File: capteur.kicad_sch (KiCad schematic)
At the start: 14 parts, among them U1 MAX86141ENP+T, U2 ICM-20948

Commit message: Routage complet
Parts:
- removed C3: 100n, symbol Device:C
- removed D4, D5: VEMD5080X01, symbol Device:D_Photo
- removed U2: ICM-20948, Sensor_Motion:InvenSense_QFN-24_3x3mm_P0.4mm, symbol Sensor_Motion:ICM-20948
- added C31: 10n, Capacitor_SMD:C_0805_2012Metric, symbol Device:C
- added C33: 10µ, Capacitor_SMD:C_0805_2012Metric, symbol Device:C
- added D4, D6: VEMD8080, Local:XDCR_VEMD8080, symbol VEMD8080:VEMD8080
- added JP1: SolderJumper_2_Bridged, Jumper:SolderJumper-2_P1.3mm_Bridged2Bar_RoundedPad1.0x1.5mm, symbol Jumper:SolderJumper_2_Bridged
- added MT1: ICM-42670-P, Local:XDCR_ICM-42670-P, symbol ICM-42670-P:ICM-42670-P
- C1, C4, C5, C6, C7: footprint (none) -> Capacitor_SMD:C_0805_2012Metric
- C2: value 100n -> 2.2µ; footprint (none) -> Capacitor_SMD:C_0805_2012Metric
- D1, D2, D3: footprint (none) -> Local:CTDBLP31126C5D56J6U620R18
- U1: footprint 21-100134_N201A2-1_MXM -> Local:21-100134_N201A2-1_MXM
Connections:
- net +3.3V: now also C31.1, C33.1, MT1.12 (AP_CS), MT1.5 (VDDIO), MT1.8 (VDD)
- net GND: now also C31.2, JP1.2 (B), MT1.6 (GND); no longer U1.C5 (PD_GND)
- net ICM_AD0: now also MT1.1 (AP_SDO/AP_AD0)
- net ICM_FSYNC: now also MT1.7 (FSYNC)
- net ICM_INT: now also MT1.4 (INT1/INT)
- net SCL: now also MT1.13 (AP_SCL/AP_SCLK)
- net SDA: now also MT1.14 (AP_SDA/AP_SDIO/AP_SDI)
- net at U1.D5 (PD1_IN): now also D6.1, D6.2, D6.3, D6.4, D6.6, D6.7, D6.8
- net at U1.D4 (PD2_IN): now also D4.1, D4.2, D4.3, D4.4, D4.6, D4.7, D4.8
- net MAX_INT_1_8: no longer names the net of U1.B2 (*INT)
- new net ICM_INT2: MT1.9 (INT2)
- new net PD_GND: C33.2, D4.5, D6.5, JP1.1 (A), U1.C5 (PD_GND)
- no-connect marks 4 -> 8
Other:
- moved on the sheet: C1, C2, C5

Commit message: Set MPN
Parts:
- C1: JLCPCB Part # (none) -> CL21B104KBCNNNC; manf# CC1206KKX7R7BB105 -> CL21B104KBCNNNC
- C2: JLCPCB Part # (none) -> CL21B225KAFNNNE; manf# CC1206KKX7R7BB105 -> CL21B225KAFNNNE
- C31: JLCPCB Part # (none) -> CC0805JRNPO9BN100; manf# CC1206KKX7R7BB105 -> CC0805JRNPO9BN100
- C33, C4: JLCPCB Part # (none) -> CL21B106KPQNNNE; manf# CC1206KKX7R7BB105 -> CL21B106KPQNNNE
- C5: JLCPCB Part # (none) -> CL21B105KAFNFNE; manf# CC1206KKX7R7BB105 -> CL21B105KAFNFNE
- C6, C7: JLCPCB Part # (none) -> GRM21BZ71A226ME15L; manf# CC1206KKX7R7BB105 -> GRM21BZ71A226ME15L
- D1, D2, D3: value CT DBLP31.12-5C8C-56-J6Q6 -> CT DBLP31.12-6C5D-56-J6U6-20-R18; JLCPCB Part # (none) -> CT DBLP31.12-6C5D-56-J6U6-20-R18; manf# (none) -> CT DBLP31.12-6C5D-56-J6U6-20-R18
- D4, D6: JLCPCB Part # (none) -> VEMD8080; manf# (none) -> VEMD8080
- MT1: JLCPCB Part # (none) -> ICM-42670-P; manf# (none) -> ICM-42670-P
- U1: JLCPCB Part # (none) -> MAX86141ENP+T; manf# (none) -> MAX86141ENP+T
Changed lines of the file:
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@@
+			)
+		)
+		(property "manf#" "VEMD8080"
+			(at 167.64 152.4 90)
+			(effects
+				(font
+					(size 1.27 1.27)
+				)
+				(hide yes)
+			)
+		)
+		(property "JLCPCB Part #" "VEMD8080"
+			(at 167.64 152.4 90)
+			(effects
+				(font
+					(size 1.27 1.27)
+				)
+				(hide yes)
 			)
 		)
@@
 			)
 		)
+		(property "JLCPCB Part #" ""
+			(at 49.53 182.88 0)
+			(effects
+				(font
+					(size 1.27 1.27)
+				)
+				(hide yes)
+			)
+		)
 		(pin "1"
 		)
@@
 			)
 		)
-		(property "manf#" " CC1206KKX7R7BB105"
+		(property "manf#" "CL21B105KAFNFNE"
 			(at 130.81 104.14 0)
 			(effects
@@
 		)
 		(property "gp" " CC1206KKX7R7BB105"
+			(at 130.81 104.14 0)
+			(effects
+				(font
+					(size 1.27 1.27)
+				)
+				(hide yes)
+			)
+		)
+		(property "JLCPCB Part #" "CL21B105KAFNFNE"
 			(at 130.81 104.14 0)
 			(effects
@@
 			)
 		)
-		(property "manf#" " CC1206KKX7R7BB105"
+		(property "manf#" "CL21B106KPQNNNE"
 			(at 55.88 128.27 0)
 			(effects
@@
 		)
 		(property "gp" " CC1206KKX7R7BB105"
+			(at 55.88 128.27 0)
+			(effects
+				(font
+					(size 1.27 1.27)
+				)
+				(hide yes)
+			)
+		)
+		(property "JLCPCB Part #" "CL21B106KPQNNNE"
 			(at 55.88 128.27 0)
 			(effects
@@
 			)
 		)
-		(property "manf#" " CC1206KKX7R7BB105"
+		(property "manf#" "CL21B104KBCNNNC"
 			(at 129.54 29.21 0)
 			(effects
@@
 			)
 		)
+		(property "JLCPCB Part #" "CL21B104KBCNNNC"
+			(at 129.54 29.21 0)
+			(effects
+				(font
+					(size 1.27 1.27)
+				)
+				(hide yes)
+			)
+		)
 		(pin "2"
 		)
@@
 			)
 		)
-		(property "Value" "CT DBLP31.12-5C8C-56-J6Q6"
+		(property "Value" "CT DBLP31.12-6C5D-56-J6U6-20-R18"
 			(at 196.342 130.556 0)
 			(effects
@@
 		)
 		(property "Sim.Pins" "1=K 2=A"
+			(at 199.39 130.81 0)
+			(effects
+				(font
+					(size 1.27 1.27)
+				)
+				(hide yes)
+			)
+		)
+		(property "manf#" "CT DBLP31.12-6C5D-56-J6U6-20-R18"
+			(at 199.39 130.81 0)
+			(effects
+				(font
+					(size 1.27 1.27)
+				)
+				(hide yes)
+			)
+		)
+		(property "JLCPCB Part #" "CT DBLP31.12-6C5D-56-J6U6-20-R18"
 			(at 199.39 130.81 0)
 			(effects
@@
 			)
 		)
-		(property "Value" "CT DBLP31.12-5C8C-56-J6Q6"
+		(property "Value" "CT DBLP31.12-6C5D-56-J6U6-20-R18"
 			(at 186.182 130.556 0)
 			(effects
@@
 			)
 		)
+		(property "manf#" "CT DBLP31.12-6C5D-56-J6U6-20-R18"
+			(at 189.23 130.81 0)
+			(effects
+				(font
+					(size 1.27 1.27)
+				)
+				(hide yes)
+			)
+		)
+		(property "JLCPCB Part #" "CT DBLP31.12-6C5D-56-J6U6-20-R18"
+			(at 189.23 130.81 0)
+			(effects
+				(font
+					(size 1.27 1.27)
+				)
+				(hide yes)
+			)
+		)
 		(pin "2"
 		)
@@
 		)
 		(property "Description" ""
+			(at 104.14 137.16 0)
+			(effects
+				(font
+					(size 1.27 1.27)
+				)
+				(hide yes)
+			)
+		)
+		(property "JLCPCB Part #" "MAX86141ENP+T"
+			(at 104.14 137.16 0)
+			(effects
+				(font
+					(size 1.27 1.27)
+				)
+				(hide yes)
+			)
+		)
+		(property "manf#" "MAX86141ENP+T"
 			(at 104.14 137.16 0)
 			(effects
@@
 			)
 		)
-		(property "Value" "CT DBLP31.12-5C8C-56-J6Q6"
+		(property "Value" "CT DBLP31.12-6C5D-56-J6U6-20-R18"
 			(at 207.772 130.556 0)
 			(effects
@@
 		)
 		(property "Sim.Pins" "1=K 2=A"
+			(at 210.82 130.81 0)
+			(effects
+				(font
+					(size 1.27 1.27)
+				)
+				(hide yes)
+			)
+		)
+		(property "manf#" "CT DBLP31.12-6C5D-56-J6U6-20-R18"
+			(at 210.82 130.81 0)
+			(effects
+				(font
+					(size 1.27 1.27)
+				)
+				(hide yes)
+			)
+		)
+		(property "JLCPCB Part #" "CT DBLP31.12-6C5D-56-J6U6-20-R18"
 			(at 210.82 130.81 0)
 			(effects
@@
 			)
 		)
-		(property "manf#" " CC1206KKX7R7BB105"
+		(property "manf#" "CL21B106KPQNNNE"
 			(at 220.98 130.81 0)
 			(effects
@@
 		)
 		(property "gp" " CC1206KKX7R7BB105"
+			(at 220.98 130.81 0)
+			(effects
+				(font
+					(size 1.27 1.27)
+				)
+				(hide yes)
+			)
+		)
+		(property "JLCPCB Part #" "CL21B106KPQNNNE"
 			(at 220.98 130.81 0)
 			(effects
@@
 			)
 		)
+		(property "manf#" "VEMD8080"
+			(at 144.78 152.4 90)
+			(effects
+				(font
+					(size 1.27 1.27)
+				)
+				(hide yes)
+			)
+		)
+		(property "JLCPCB Part #" "VEMD8080"
+			(at 144.78 152.4 90)
+			(effects
+				(font
+					(size 1.27 1.27)
+				)
+				(hide yes)
+			)
+		)
 		(pin "5"
 		)
@@
 			)
 		)
-		(property "manf#" " CC1206KKX7R7BB105"
+		(property "manf#" "CC0805JRNPO9BN100"
 			(at 93.98 29.21 0)
 			(effects
@@
 		)
 		(property "gp" " CC1206KKX7R7BB105"
+			(at 93.98 29.21 0)
+			(effects
+				(font
+					(size 1.27 1.27)
+				)
+				(hide yes)
+			)
+		)
+		(property "JLCPCB Part #" "CC0805JRNPO9BN100"
 			(at 93.98 29.21 0)
 			(effects
@@
 			)
 		)
-		(property "manf#" " CC1206KKX7R7BB105"
+		(property "manf#" "GRM21BZ71A226ME15L"
 			(at 72.39 107.95 0)
 			(effects
@@
 		)
 		(property "gp" " CC1206KKX7R7BB105"
+			(at 72.39 107.95 0)
+			(effects
+				(font
+					(size 1.27 1.27)
+				)
+				(hide yes)
+			)
+		)
+		(property "JLCPCB Part #" "GRM21BZ71A226ME15L"
 			(at 72.39 107.95 0)
 			(effects
@@
 			)
 		)
-		(property "manf#" " CC1206KKX7R7BB105"
+		(property "manf#" "GRM21BZ71A226ME15L"
 			(at 82.55 107.95 0)
 			(effects
@@
 			)
 		)
+		(property "JLCPCB Part #" "GRM21BZ71A226ME15L"
+			(at 82.55 107.95 0)
+			(effects
+				(font
+					(size 1.27 1.27)
+				)
+				(hide yes)
+			)
+		)
 		(pin "2"
 		)
@@
 				)
 				(justify bottom)
+				(hide yes)
+			)
+		)
+		(property "JLCPCB Part #" "ICM-42670-P"
+			(at 109.22 58.42 0)
+			(effects
+				(font
+					(size 1.27 1.27)
+				)
+				(hide yes)
+			)
+		)
+		(property "manf#" "ICM-42670-P"
+			(at 109.22 58.42 0)
+			(effects
+				(font
+					(size 1.27 1.27)
+				)
 				(hide yes)
 			)
@@
 			)
 		)
-		(property "manf#" " CC1206KKX7R7BB105"
+		(property "manf#" "CL21B225KAFNNNE"
 			(at 140.97 29.21 0)
 			(effects
@@
 			(at 140.97 29.21 0)
 			(effects
+				(font
+					(size 1.27 1.27)
+				)
+				(hide yes)
+			)
+		)
+		(property "JLCPCB Part #" "CL21B225KAFNNNE"
+			(at 140.97 29.21 0)
+			(effects

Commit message: Change Code for JLC part
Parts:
- C1: JLCPCB Part # CL21B104KBCNNNC -> C1711
- C2: JLCPCB Part # CL21B225KAFNNNE -> C19110
- C31: JLCPCB Part # CC0805JRNPO9BN100 -> C107107
- C33, C4: JLCPCB Part # CL21B106KPQNNNE -> C32635
- C5: JLCPCB Part # CL21B105KAFNFNE -> C1712
- C6, C7: JLCPCB Part # GRM21BZ71A226ME15L -> C907991
- D1, D2, D3: JLCPCB Part # CT DBLP31.12-6C5D-56-J6U6-20-R18 -> C5344735
- D4, D6: JLCPCB Part # VEMD8080 -> C511402
- MT1: JLCPCB Part # ICM-42670-P -> C3288646
- U1: JLCPCB Part # MAX86141ENP+T -> C5328762
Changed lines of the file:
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@@
 			)
 		)
-		(property "JLCPCB Part #" "VEMD8080"
+		(property "JLCPCB Part #" "C511402"
 			(at 167.64 152.4 90)
 			(effects
@@
 			)
 		)
-		(property "JLCPCB Part #" "CL21B105KAFNFNE"
+		(property "JLCPCB Part #" "C1712"
 			(at 130.81 104.14 0)
 			(effects
@@
 			)
 		)
-		(property "JLCPCB Part #" "CL21B106KPQNNNE"
+		(property "JLCPCB Part #" "C32635"
 			(at 55.88 128.27 0)
 			(effects
@@
 			)
 		)
-		(property "JLCPCB Part #" "CL21B104KBCNNNC"
+		(property "JLCPCB Part #" "C1711"
 			(at 129.54 29.21 0)
 			(effects
@@
 			)
 		)
-		(property "JLCPCB Part #" "CT DBLP31.12-6C5D-56-J6U6-20-R18"
+		(property "JLCPCB Part #" "C5344735"
 			(at 199.39 130.81 0)
 			(effects
@@
 			)
 		)
-		(property "JLCPCB Part #" "CT DBLP31.12-6C5D-56-J6U6-20-R18"
+		(property "JLCPCB Part #" "C5344735"
 			(at 189.23 130.81 0)
 			(effects
@@
 			)
 		)
-		(property "JLCPCB Part #" "MAX86141ENP+T"
+		(property "JLCPCB Part #" "C5328762"
 			(at 104.14 137.16 0)
 			(effects
@@
 			)
 		)
-		(property "JLCPCB Part #" "CT DBLP31.12-6C5D-56-J6U6-20-R18"
+		(property "JLCPCB Part #" "C5344735"
 			(at 210.82 130.81 0)
 			(effects
@@
 			)
 		)
-		(property "JLCPCB Part #" "CL21B106KPQNNNE"
+		(property "JLCPCB Part #" "C32635"
 			(at 220.98 130.81 0)
 			(effects
@@
 			)
 		)
-		(property "JLCPCB Part #" "VEMD8080"
+		(property "JLCPCB Part #" "C511402"
 			(at 144.78 152.4 90)
 			(effects
@@
 			)
 		)
-		(property "JLCPCB Part #" "CC0805JRNPO9BN100"
+		(property "JLCPCB Part #" "C107107"
 			(at 93.98 29.21 0)
 			(effects
@@
 			)
 		)
-		(property "JLCPCB Part #" "GRM21BZ71A226ME15L"
+		(property "JLCPCB Part #" "C907991"
 			(at 72.39 107.95 0)
 			(effects
@@
 			)
 		)
-		(property "JLCPCB Part #" "GRM21BZ71A226ME15L"
+		(property "JLCPCB Part #" "C907991"
 			(at 82.55 107.95 0)
 			(effects
@@
 			)
 		)
-		(property "JLCPCB Part #" "ICM-42670-P"
+		(property "JLCPCB Part #" "C3288646"
 			(at 109.22 58.42 0)
 			(effects
@@
 			)
 		)
-		(property "JLCPCB Part #" "CL21B225KAFNNNE"
+		(property "JLCPCB Part #" "C19110"
 			(at 140.97 29.21 0)
 			(effects

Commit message: JLC code chage
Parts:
- C31: JLCPCB Part # C107107 -> C1710; manf# CC0805JRNPO9BN100 -> CL21B103KBANNNC
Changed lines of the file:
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@@
 			)
 		)
-		(property "manf#" "CC0805JRNPO9BN100"
+		(property "manf#" "CL21B103KBANNNC"
 			(at 93.98 29.21 0)
 			(effects
@@
 			)
 		)
-		(property "JLCPCB Part #" "C107107"
+		(property "JLCPCB Part #" " C1710"
 			(at 93.98 29.21 0)
 			(effects
@@
 		)
 		(property "Value" "ICM-42670-P"
-			(at 109.22 43.18 0)
-			(effects
-				(font
+			(at 101.854 76.454 0)
+			(effects
+				(font

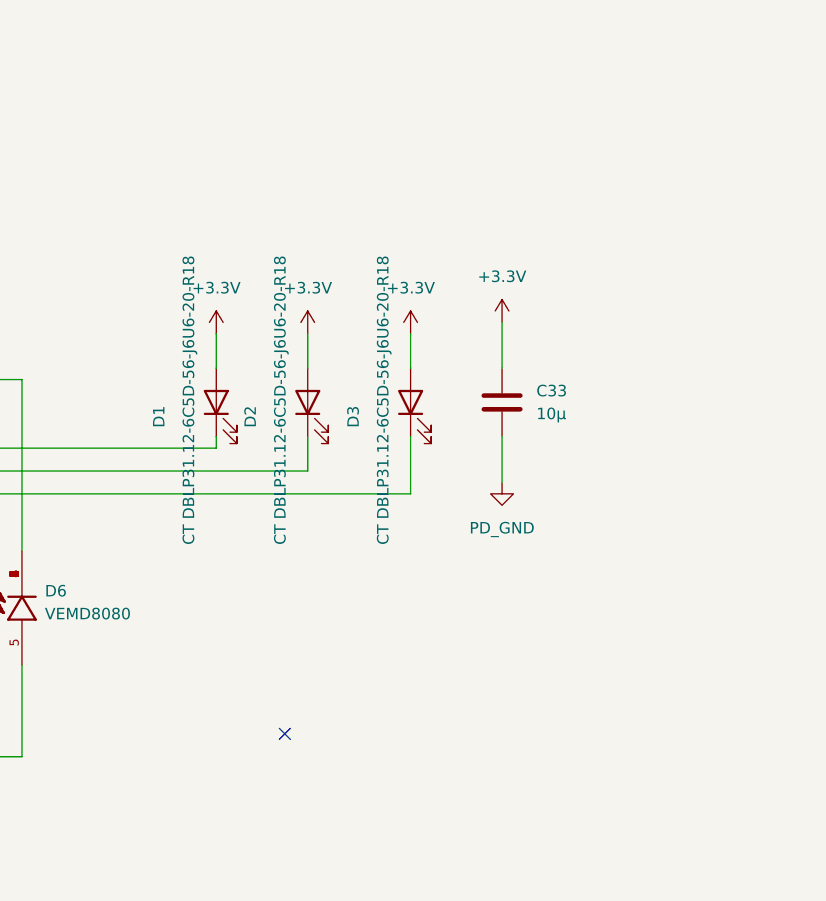
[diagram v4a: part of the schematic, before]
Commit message: Add Flash device
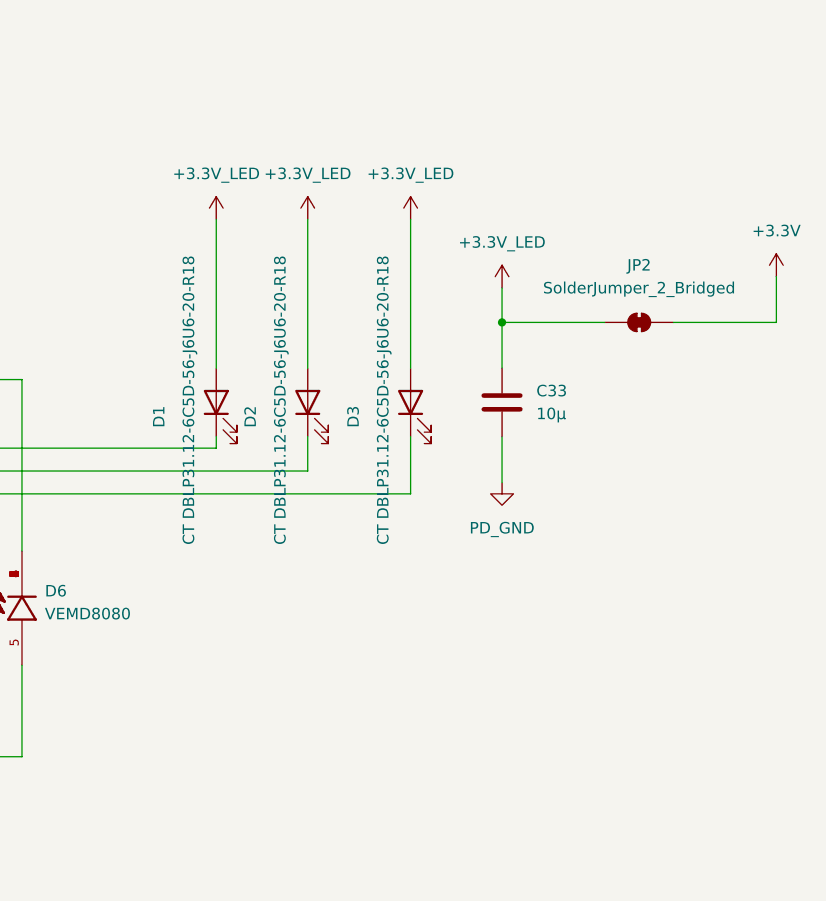
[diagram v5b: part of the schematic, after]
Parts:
- added JP2: SolderJumper_2_Bridged, Jumper:SolderJumper-2_P1.3mm_Bridged2Bar_RoundedPad1.0x1.5mm, symbol Jumper:SolderJumper_2_Bridged
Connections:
- net +3.3V: now also JP2.2 (B); no longer C33.1, D1.2 (A), D2.2 (A), D3.2 (A)
- new net +3.3V_LED: C33.1, D1.2 (A), D2.2 (A), D3.2 (A), JP2.1 (A)
- no-connect marks 8 -> 7

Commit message: Add version
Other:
- company: (none) -> Philippe12
- title: (none) -> HorseSense
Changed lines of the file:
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@@
 	(generator_version "9.0")
 	(paper "A4")
+	(title_block
+		(title "HorseSense")
+		(date "2025-11-01")
+		(rev "1.0")
+		(company "Philippe12")
+	)
 	(junction
 		(at 93.98 24.13)

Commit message: 3D export
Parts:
- C31: value 10n -> 1µ; JLCPCB Part # C1710 -> C1712; manf# CL21B103KBANNNC -> CL21B105KAFNFNE
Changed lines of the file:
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@@
 			)
 		)
-		(property "Value" "10n"
+		(property "Value" "1µ"
 			(at 97.79 30.4799 0)
 			(effects
@@
 			)
 		)
-		(property "manf#" "CL21B103KBANNNC"
+		(property "manf#" "CL21B105KAFNFNE"
 			(at 93.98 29.21 0)
 			(effects
@@
 			)
 		)
-		(property "JLCPCB Part #" " C1710"
+		(property "JLCPCB Part #" "C1712"
 			(at 93.98 29.21 0)
 			(effects
